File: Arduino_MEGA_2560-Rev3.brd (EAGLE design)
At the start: 101.6 x 53.3 mm, 63 parts, among them IC1 NCP1117ST50T3G, IC3 ATMEGA2560-16AU, IC4 ATMEGA16U2-MU, IC6 LP2985-33DBVR, IC7 LMV358IDGKR, T1 FDN340P, X1 POWERSUPPLY_DC21MMX, X2 USB-B_TH, Y1 CSTCE16M0V53-R0 16MHZ, Y2 16MHz

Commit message: Version inicial del Shield
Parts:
- removed C1, C14, C15: 22p, SmartPrj:C0603-ROUND
- removed C10, C13: 1u, SmartPrj:C0603-ROUND
- removed C11, C12, C2, C3, C4, C5, C6, C7, C8, C9: 100n, SmartPrj:C0603-ROUND
- removed D1: M7, diode:SMB
- removed D2, D3: CD1206-S01575, diode:MINIMELF
- removed F1: MF-MSMF050-2 500mA, rcl:L1812
- removed FD1, FD2, FD3, FD4: FIDUCIALMOUNT, SmartPrj:FIDUCIA-MOUNT
- removed GROUND, RESET-EN: (no value), jumper:SJ
- removed IC1: NCP1117ST50T3G, linear:SOT223
- removed IC3: ATMEGA2560-16AU, SmartPrj:TQFP100
- removed IC4: ATMEGA16U2-MU, SmartPrj:MLF32
- removed IC6: LP2985-33DBVR, SmartPrj:SOT23-DBV
- removed IC7: LMV358IDGKR, linear:MSOP08
- removed ICSP, ICSP1: 3x2M, SmartPrj:2X03
- removed JP5: 2x2M - NM, SmartPrj:2X02
- removed L, RX, TX: YELLOW, led:CHIP-LED0805
- removed L1: BLM21, wuerth-elektronik:0805
- removed ON: GREEN, led:CHIP-LED0805
- removed PC1, PC2: 47u, rcl:PANASONIC_D
- removed RESET: TS42031-160R-TR-7260, SmartPrj:TS42
- removed RN1, RN5: 10K, resistor-dil:CAT16
- removed RN2: 22R, resistor-dil:CAY16
- removed RN3, RN4: 1k, resistor-dil:CAY16
- removed T1: FDN340P, zetex:SOT-23
- removed X1: POWERSUPPLY_DC21MMX, SmartPrj:POWERSUPPLY_DC-21MM
- removed X2: USB-B_TH, SmartPrj:PN61729
- removed Y1: CSTCE16M0V53-R0 16MHZ, SmartPrj:RESONATOR
- removed Y2: 16MHz, SmartPrj:QS
- removed Z1, Z2: CG0603MLC-05E, varistor:CT/CN0603
- added LED1, LED2: (no value), led:CHIPLED_1206
- added R10, R11, R12, R13, R14, R15, R16, R17, R18, R19, R20, R3, R4, R5, R6, R7, R8, R9: (no value), resistor:M1206
- added U$2, U$3, U$4, U$5, U$6, U$7, U$8, U$9: XPORT, SparkFun-Boards:XPORT
- R1, R2: value 1M -> (none); device SmartPrj:R0603-ROUND -> resistor:M1206
- U$1: value DISCLAIMER -> XPORT; device SmartPrj:DISCLAIMER -> SparkFun-Boards:XPORT
- moved R2 84.4 mm to (95.7, 63.2), turned to 180 degrees
- moved R1 76.0 mm to (95.7, 66.9), turned to 0 degrees
- moved U$1 48.7 mm to (14.2, 13.8)
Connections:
- removed net 5-GND: RESET.5
- removed net 8PB4: IC4.18, JP5.1
- removed net 8PB5: IC4.19, JP5.3
- removed net 8PB6: IC4.20, JP5.2
- removed net 8PB7: IC4.21, JP5.4
- removed net ADC0: ADCL.1, IC3.97
- removed net ADC1: ADCL.2, IC3.96
- removed net ADC10: ADCH.3, IC3.87
- removed net ADC11: ADCH.4, IC3.86
- removed net ADC12: ADCH.5, IC3.85
- removed net ADC13: ADCH.6, IC3.84
- removed net ADC14: ADCH.7, IC3.83
- removed net ADC15: ADCH.8, IC3.82
- removed net ADC2: ADCL.3, IC3.95
- removed net ADC3: ADCL.4, IC3.94
- removed net ADC4: ADCL.5, IC3.93
- removed net ADC5: ADCL.6, IC3.92
- removed net ADC6: ADCL.7, IC3.91
- removed net ADC7: ADCL.8, IC3.90
- removed net ADC8: ADCH.1, IC3.89
- removed net ADC9: ADCH.2, IC3.88
- removed net CMP: C12.2, IC7.5, RN5.3, RN5.5
- removed net D+: RN2.5, X2.3, Z2.2
- removed net D-: RN2.8, X2.2, Z1.2
- removed net DTR: C7.1, IC4.13, RN3.4
- removed net GATE_CMD: IC7.7, T1.3
- removed net L13: IC7.1, IC7.2, RN3.7
- removed net M8RXD: IC4.9, RN4.7
- removed net M8TXD: IC4.8, RN4.8
- removed net MISO2: IC4.17, ICSP1.1
- removed net MOSI2: IC4.16, ICSP1.4
- removed net N$54: RN4.4, RX.A
- removed net N$55: RN4.3, TX.A
- removed net PWRIN: D1.A, X1.2
- removed net RD+: IC4.29, RN2.4
- removed net RD-: IC4.30, RN2.1
- removed net RESET2: D2.A, IC4.24, ICSP1.5, RN5.7
- removed net RXL: IC4.10, RX.C
- removed net SCK2: IC4.15, ICSP1.3
- removed net TXL: IC4.11, TX.C
- removed net UGND: C10.2, GROUND.1, IC4.28, L1.1, X2.4
- removed net USBVCC: C8.1, F1.1, IC4.31, T1.1
- removed net USHIELD: L1.2, X2.P$1, X2.P$2, Z1.1, Z2.1
- removed net VUCAP: C10.1, IC4.27
- removed net XT1: C14.1, IC4.1, R2.1, Y2.2
- removed net XT2: C15.1, IC4.2, R2.2, Y2.1
- removed net XTAL1: IC3.34, R1.1, Y1.3
- removed net XTAL2: IC3.33, R1.2, Y1.1
- removed net XVCC: F1.2, X2.1
- new net N$1: LED1.A, R1.1
- new net N$10: ADCH.3, R7.2
- new net N$11: ADCL.4, R14.2
- new net N$12: ADCL.5, R15.2
- new net N$13: ADCL.6, R16.2
- new net N$14: ADCL.7, R17.2
- new net N$15: ADCL.8, R18.2
- new net N$16: R12.1, U$8.P7
- new net N$17: R13.1, U$8.P6
- new net N$18: R14.1, U$8.P5
- new net N$19: R15.1, U$8.P4
- new net N$20: R16.1, U$8.P3
- new net N$21: ADCH.4, R8.2
- new net N$22: ADCH.5, R9.2
- new net N$23: ADCH.6, R10.2
- new net N$24: ADCH.7, R4.2
- new net N$25: ADCH.8, R3.2
- new net N$26: R17.1, U$2.P8
- new net N$27: R18.1, U$2.P7
- new net N$28: R5.1, U$2.P6
- new net N$29: R6.1, U$2.P5
- new net N$30: R7.1, U$2.P4
- new net N$31: R8.1, U$2.P3
- new net N$32: R9.1, U$3.P8
- new net N$33: R10.1, U$3.P7
- new net N$34: R4.1, U$3.P6
- new net N$35: R3.1, U$3.P5
- new net N$36: R19.1, U$3.P3
- new net N$37: R20.2, XIO.33
- new net N$4: ADCH.2, R6.2
- new net N$5: JP6.2
- new net N$6: R11.1, U$8.P8
- new net N$7: ADCL.1, R11.2
- new net N$8: ADCL.2, R12.2
- new net N$9: ADCL.3, R13.2
- net +3V3: no longer C13.2, IC6.5, IC7.6
- net +5V: now also R1.2, R2.2; no longer C11.2, C4.1, C5.1, C6.1, C9.1, D2.C, D3.C, IC1.2, IC1.4, IC3.10, IC3.100, IC3.31, IC3.61, IC3.80, IC4.32, IC4.4, IC6.1, IC6.3, IC7.8, ICSP.2, ICSP1.2, PC2.+, RN1.6, RN1.7, RN3.1, RN4.5, RN4.6, RN5.2, RN5.8, T1.2
- net AREF: no longer C3.1, IC3.98
- net GND: now also LED1.C, LED2.C, U$1.P1, U$1.P2, U$2.P1, U$2.P2, U$3.P1, U$3.P2, U$4.P1, U$4.P2, U$5.P1, U$5.P2, U$6.P1, U$6.P2, U$7.P1, U$7.P2, U$8.P1, U$8.P2, U$9.P1, U$9.P2; no longer C1.2, C11.1, C12.1, C13.1, C14.2, C15.2, C2.2, C3.2, C4.2, C5.2, C6.2, C8.2, C9.2, GROUND.2, IC1.1, IC3.11, IC3.32, IC3.62, IC3.81, IC3.99, IC4.3, IC4.33, IC6.2, IC7.4, ICSP.6, ICSP1.6, L.C, ON.C, PC1.-, PC2.-, RESET.1, RESET.2, RN3.5, RN5.4, X1.1, X1.3, Y1.2
- net N$2: now also LED2.A, R2.1; no longer L.A, RN3.2
- net N$3: now also ADCH.1, R5.2; no longer ON.A, RN3.8
- net PA0: no longer IC3.78
- net PA1: no longer IC3.77
- net PA2: no longer IC3.76
- net PA3: no longer IC3.75
- net PA4: no longer IC3.74
- net PA5: no longer IC3.73
- net PA6: no longer IC3.72
- net PA7: no longer IC3.71
- net PB0: now also R19.2; no longer IC3.19
- net PB1: now also R20.1, U$3.P4; no longer IC3.20, ICSP.3, XIO.33
- net PB2: no longer IC3.21, ICSP.4
- net PB3: no longer IC3.22, ICSP.1
- net PB4: no longer IC3.23
- net PB5: no longer IC3.24
- net PB6: no longer IC3.25
- net PB7: no longer IC3.26, IC7.3
- net PC0: no longer IC3.53
- net PC1: no longer IC3.54
- net PC2: no longer IC3.55
- net PC3: no longer IC3.56
- net PC4: no longer IC3.57
- net PC5: no longer IC3.58
- net PC6: no longer IC3.59
- net PC7: no longer IC3.60
- net PD7: no longer IC3.50
- net PE0: no longer IC3.2, RN4.2
- net PE1: no longer IC3.3, RN4.1
- net PE3: no longer IC3.5
- net PE4: no longer IC3.6
- net PE5: no longer IC3.7
- net PG0: no longer IC3.51
- net PG1: no longer IC3.52
- net PG2: no longer IC3.70
- net PG5: no longer IC3.1
- net PH3: no longer IC3.15
- net PH4: no longer IC3.16
- net PH5: no longer IC3.17
- net PH6: no longer IC3.18
- net PL0: no longer IC3.35
- net PL1: no longer IC3.36
- net PL2: no longer IC3.37
- net PL3: no longer IC3.38
- net PL4: no longer IC3.39
- net PL5: no longer IC3.40
- net PL6: no longer IC3.41
- net PL7: no longer IC3.42
- net RESET: no longer C1.1, C7.2, D3.A, IC3.30, ICSP.5, RESET-EN.1, RESET-EN.2, RESET.3, RESET.4, RN5.1
- net RXD1: no longer IC3.45
- net RXD2: no longer IC3.12
- net RXD3: no longer IC3.63
- net SCL: no longer IC3.43, RN1.2
- net SDA: no longer IC3.44, JP6.2, RN1.3
- net TXD1: no longer IC3.46
- net TXD2: no longer IC3.13
- net TXD3: no longer IC3.64
- net VIN: no longer C2.1, D1.C, IC1.3, PC1.+, RN5.6
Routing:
- net +5V: track 345.6 -> 0.00 mm, vias 24 -> 0
- net SCL: track 167.8 -> 0.00 mm, vias 4 -> 0
- net SDA: track 158.9 -> 0.00 mm, vias 4 -> 0
- net RESET: track 158.1 -> 0.00 mm, vias 6 -> 0
- net PB3: track 115.4 -> 0.00 mm, vias 3 -> 0
- net PB2: track 104.5 -> 0.00 mm, vias 3 -> 0
- net PB1: track 91.3 -> 0.00 mm, vias 3 -> 0
- net ADC13: track 75.2 -> 0.00 mm, vias 1 -> 0
- net ADC14: track 72.8 -> 0.00 mm, vias 1 -> 0
- net N$3: track 72.5 -> 0.00 mm, vias 4 -> 0
- net ADC11: track 71.2 -> 0.00 mm, vias 1 -> 0
- net ADC12: track 71.0 -> 0.00 mm, vias 1 -> 0
- net ADC15: track 70.6 -> 0.00 mm, vias 1 -> 0
- net PB0: track 66.4 -> 0.00 mm, vias 2 -> 0
- net PB7: track 65.1 -> 0.00 mm, vias 1 -> 0
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- removed copper zone on layer 1, net +5V
- removed copper zone on layer 16, net +5V
- removed copper zone on layer 1, net GND
- removed copper zone on layer 16, net GND
- removed copper zone on layer 1, net N$1
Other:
- board size 101.6 x 53.3 mm -> 101.6 x 72.2 mm
- board text removed: "ANALOG IN"
- board text removed: "ITALY"
- board text removed: "MADE IN"
- board text removed: "PWM"
- board text removed: "designed by"
- board text removed: "tinker it"

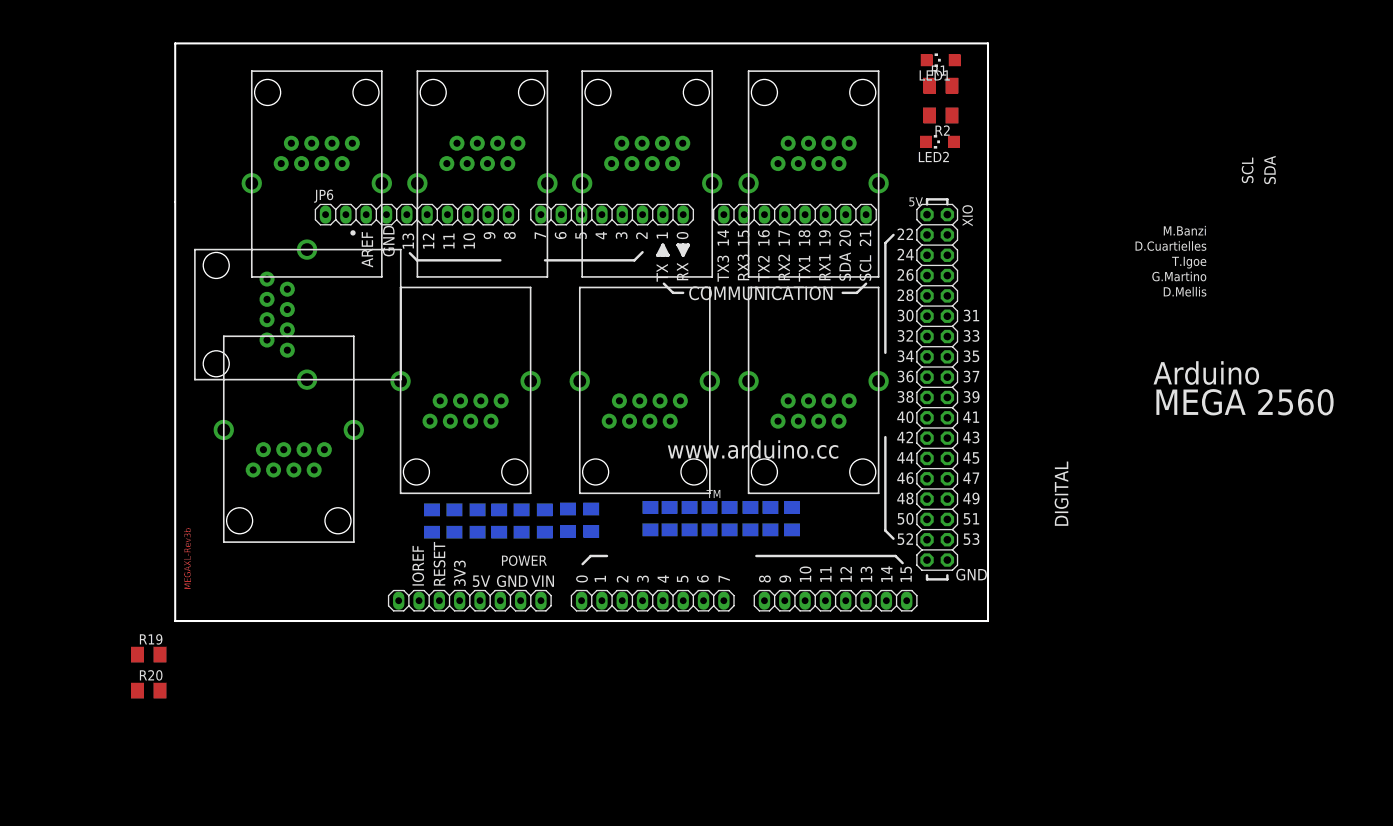
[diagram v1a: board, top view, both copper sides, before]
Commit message: nuevas dimensiones placa
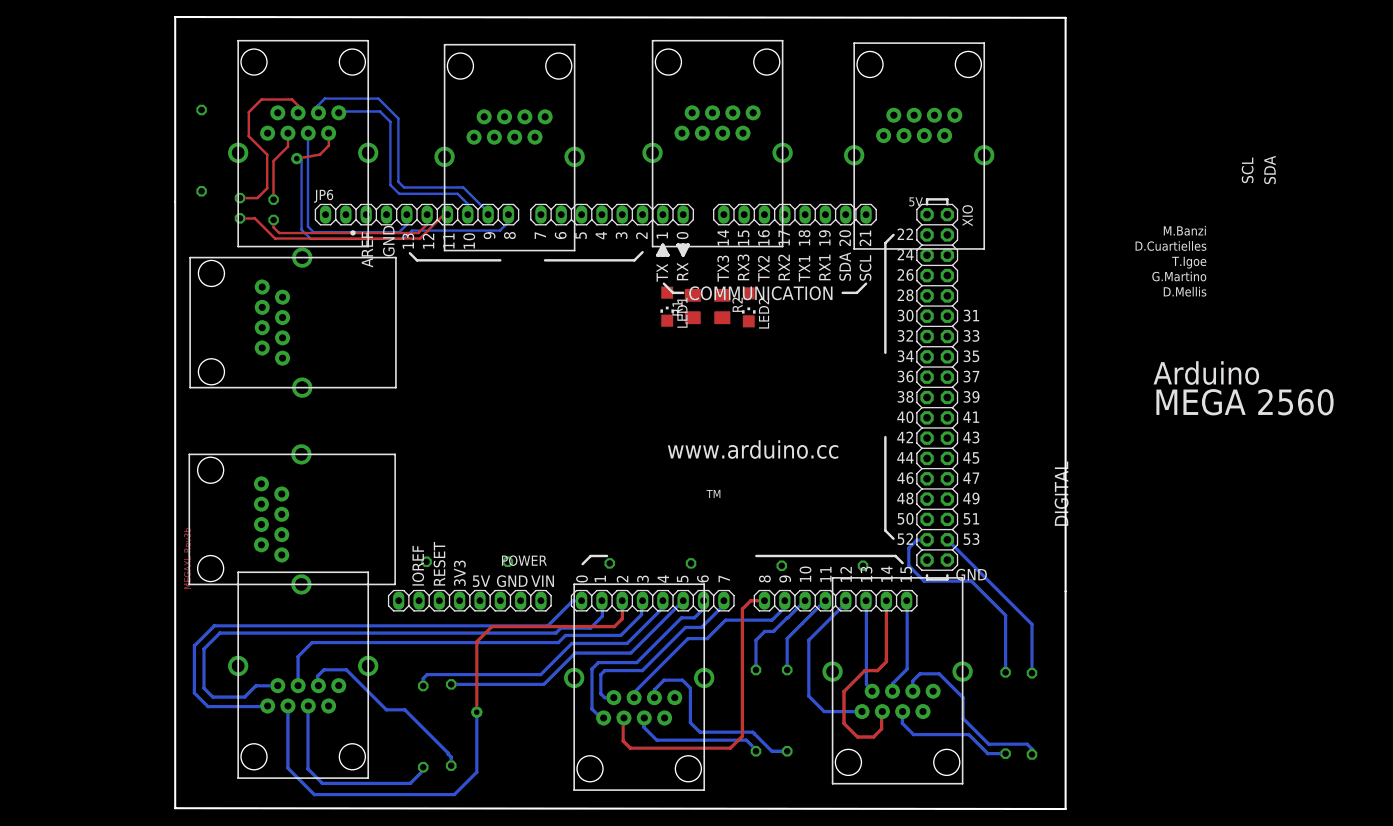
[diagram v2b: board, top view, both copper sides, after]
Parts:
- removed R10, R16, R17, R18, R4, R5, R6, R9: (no value), resistor:M1206
- added R21, R25: (no value), rcl:0207/2V
- R11, R12, R13, R14, R15, R19, R20, R3, R7, R8: device resistor:M1206 -> rcl:0207/10
- moved R19 110.6 mm to (107.1, -11.6), flipped to the bottom, turned to 90 degrees
- moved R20 107.1 mm to (103.8, -11.5), flipped to the bottom, turned to 90 degrees
- moved R14 59.4 mm to (3.30, 58.8)
- moved LED1 46.0 mm to (61.5, 39.3), turned to 180 degrees
- moved R1 41.5 mm to (64.7, 39.3), turned to 90 degrees
- moved U$8 41.0 mm to (16.0, -15.7)
- moved U$3 37.8 mm to (90.3, -16.4)
- moved U$2 37.1 mm to (58.0, -17.2)
- moved R2 36.3 mm to (68.4, 39.3), turned to 270 degrees
- moved LED2 31.6 mm to (71.7, 39.2), turned to 180 degrees
- moved R12 26.0 mm to (31.0, -13.2), turned to 90 degrees
- moved R8 25.9 mm to (76.5, -11.2), turned to 90 degrees
- moved R11 25.6 mm to (34.5, -13.0), turned to 90 degrees
- moved R7 25.4 mm to (72.6, -11.2), turned to 90 degrees
- moved R15 16.9 mm to (59.4, 7.20), turned to 180 degrees
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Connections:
- removed net N$18: R14.1, U$8.P5
- removed net N$19: R15.1, U$8.P4
- removed net N$20: R16.1, U$8.P3
- removed net N$26: R17.1, U$2.P8
- removed net N$27: R18.1, U$2.P7
- removed net N$28: R5.1, U$2.P6
- removed net N$29: R6.1, U$2.P5
- removed net N$32: R9.1, U$3.P8
- removed net N$33: R10.1, U$3.P7
- removed net N$34: R4.1, U$3.P6
- removed net N$35: R3.1, U$3.P5
- new net N$38: R21.2, U$7.P4
- new net N$39: R25.1, U$7.P3
- new net N$44: R11.1, U$8.P3
- new net N$45: R12.1, U$8.P4
- new net N$46: R13.2, U$8.P1, U$8.P2
- net GND: now also R13.1, R14.2, R15.1, R3.2; no longer U$2.P1, U$2.P2, U$3.P1, U$3.P2, U$7.P1, U$7.P2, U$8.P1, U$8.P2
- net N$11: now also U$8.P5; no longer R14.2
- net N$12: now also R12.2; no longer R15.2
- net N$13: now also R11.2; no longer R16.2
- net N$14: now also U$2.P8; no longer R17.2
- net N$15: now also U$2.P7; no longer R18.2
- net N$16: now also R15.2, U$2.P1, U$2.P2; no longer R12.1, U$8.P7
- net N$17: now also R3.1, U$3.P1, U$3.P2; no longer R13.1, U$8.P6
- net N$22: now also U$3.P8; no longer R9.2
- net N$23: now also U$3.P7; no longer R10.2
- net N$24: now also U$3.P6; no longer R4.2
- net N$25: now also U$3.P5; no longer R3.2
- net N$3: now also U$2.P6; no longer R5.2
- net N$4: now also U$2.P5; no longer R6.2
- net N$6: now also R14.1, U$7.P1, U$7.P2; no longer R11.1, U$8.P8
- net N$7: now also U$8.P8; no longer R11.2
- net N$8: now also U$8.P7; no longer R12.2
- net N$9: now also U$8.P6; no longer R13.2
- net PB2: now also U$1.P7
- net PB3: now also U$1.P8
- net PB4: now also U$7.P8
- net PB5: now also R21.1
- net PB6: now also R25.2
- net PB7: now also U$7.P5
- net PG0: now also U$9.P3
- net PG1: now also U$9.P4
- net PH5: now also U$7.P7
- net PH6: now also U$7.P6
- net PL0: now also U$1.P5
- net PL1: now also U$1.P6
- net PL2: now also U$1.P3
- net PL3: now also U$1.P4
- net PL4: now also U$9.P7
- net PL5: now also U$9.P8
- net PL6: now also U$9.P5
- net PL7: now also U$9.P6
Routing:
- net N$9: track 0.00 -> 71.9 mm, vias 0 -> 1
- net N$8: track 0.00 -> 69.0 mm
- net N$7: track 0.00 -> 66.9 mm
- net N$11: track 0.00 -> 50.5 mm
- net PH5: track 0.00 -> 43.6 mm, vias 0 -> 1
- net N$3: track 0.00 -> 37.9 mm
- net N$12: track 0.00 -> 35.5 mm
- net PH6: track 0.00 -> 33.4 mm
- net N$13: track 0.00 -> 33.3 mm
- net PB5: track 0.00 -> 28.2 mm
- net PB4: track 0.00 -> 27.0 mm
- net N$37: track 0.00 -> 26.7 mm
- net N$24: track 0.00 -> 26.5 mm
- net PB7: track 0.00 -> 26.0 mm
- net N$14: track 0.00 -> 25.0 mm
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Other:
- board size 101.6 x 72.2 mm -> 111.3 x 99 mm
